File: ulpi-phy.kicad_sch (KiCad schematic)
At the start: 18 parts, among them U1501 USB3320C-EZK-TR, Y1503 Resonator_24MHz_ECX-1247

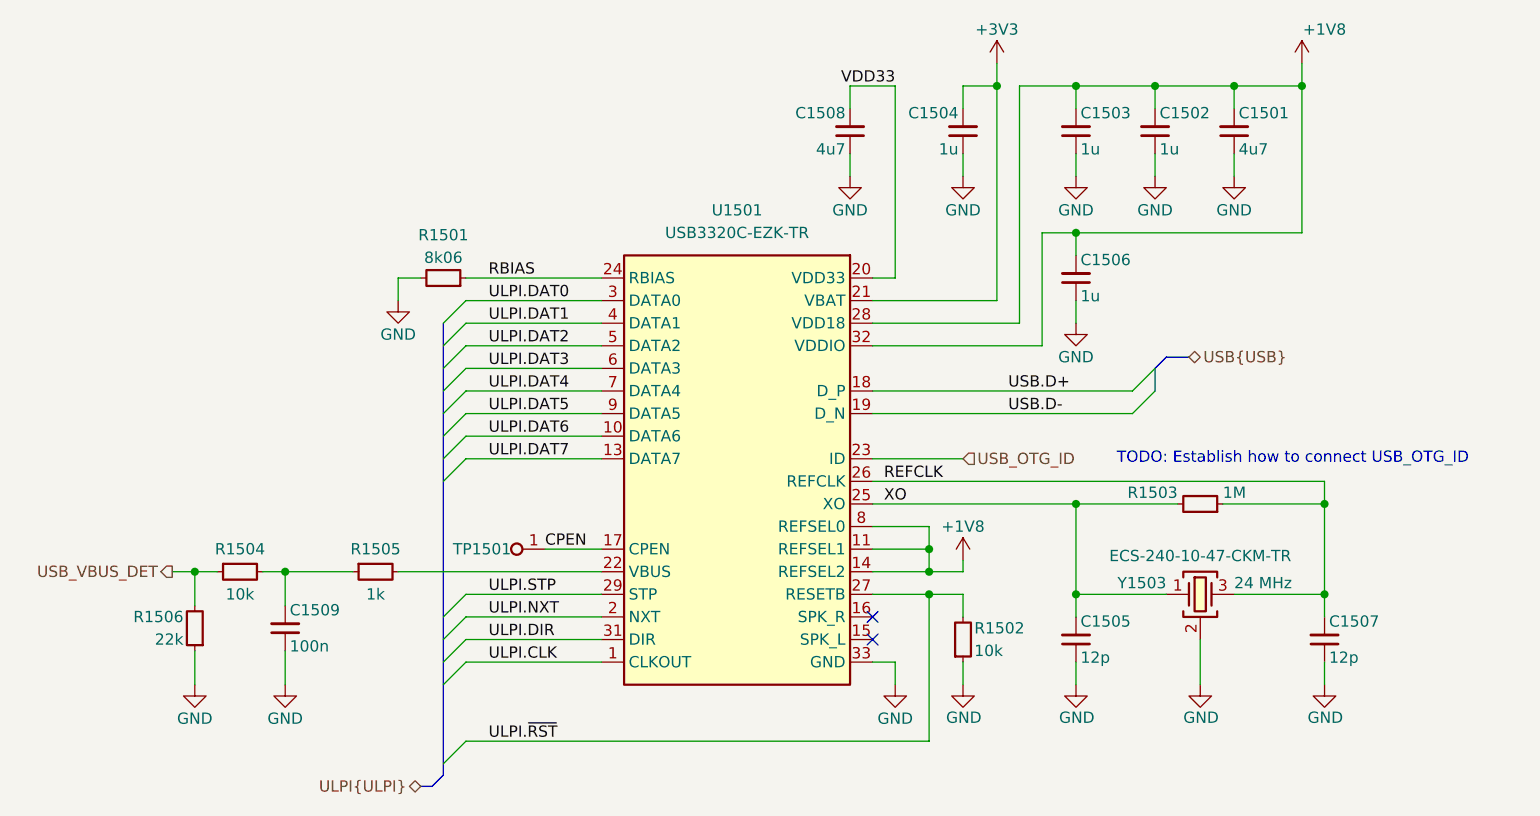
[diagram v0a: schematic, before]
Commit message: [#99852] Connect USB ID, VBUS detect, PPONx and OCIxB signals
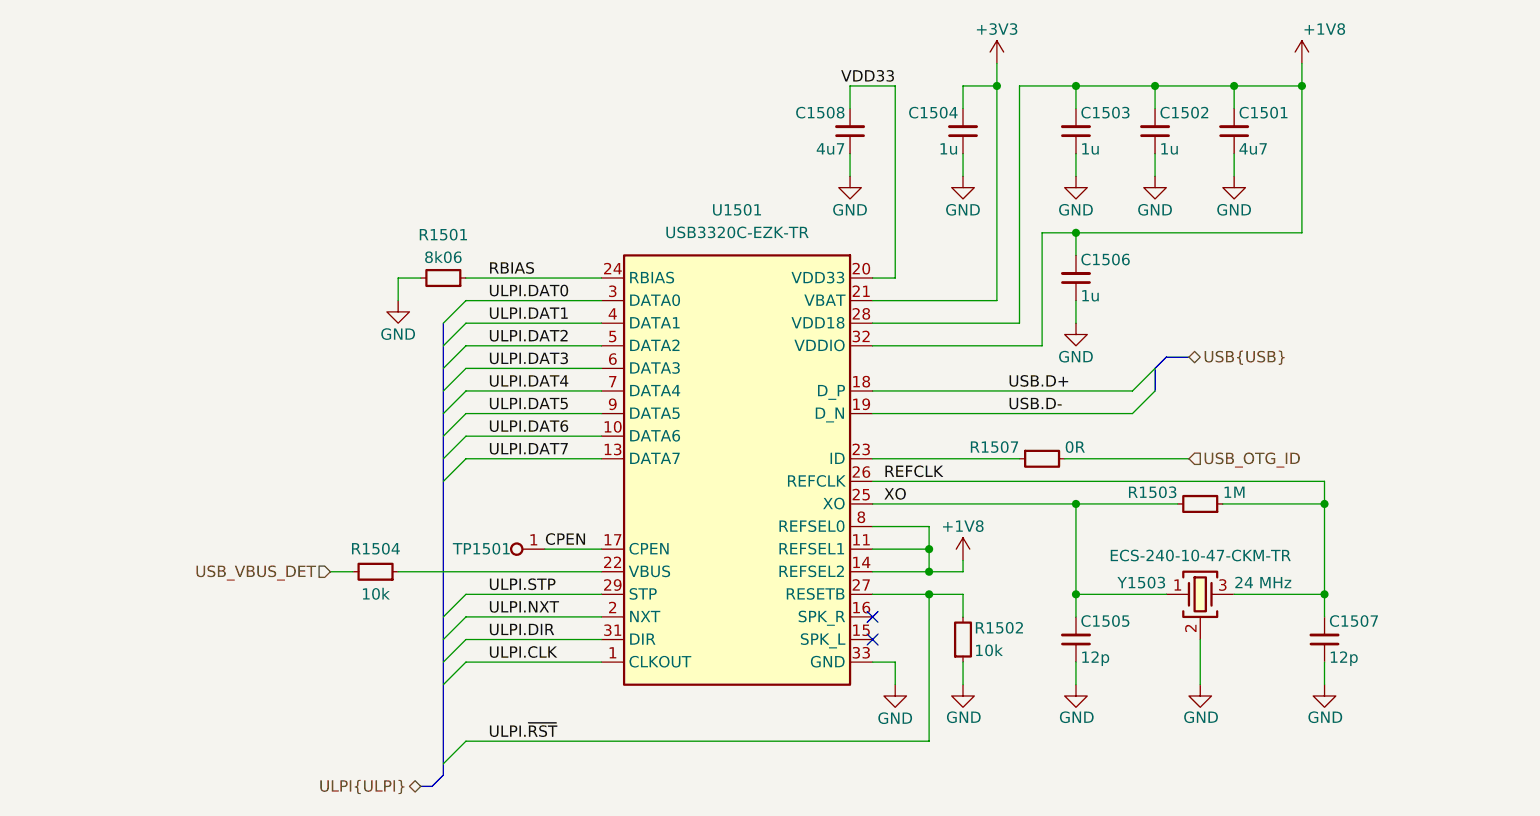
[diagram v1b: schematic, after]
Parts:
- removed C1509: C_100n_0402, antmicro-footprints:C_0402_1005Metric, symbol antmicroCapacitors0402:C_100n_0402
- removed R1505: R_1k_0402, antmicro-footprints:R_0402_1005Metric, symbol antmicroResistors0402:R_1k_0402
- removed R1506: R_22k_0402, antmicro-footprints:R_0402_1005Metric, symbol antmicroResistors0402:R_22k_0402
- added R1507: R_0R_0402, antmicro-footprints:R_0402_1005Metric, symbol antmicroResistors0402:R_0R_0402
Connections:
- net USB_OTG_ID: now also R1507.2; no longer U1501.23 (ID)
- net USB_VBUS_DET: now also R1504.2; no longer R1504.1
- net at U1501.22 (VBUS): now also R1504.1
- new net: R1507.1, U1501.23 (ID)
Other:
- note removed: "TODO: Establish how to connect USB_OTG_ID"
